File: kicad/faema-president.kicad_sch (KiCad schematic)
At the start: 18 parts, among them J1 AC_INPUT, J2 CALDEIRA_2400W, J3 PT100_CALDEIRA, J6 PT100_GRUPO, J7 SONDA_NIVEL, U1 ESP32-S3 Mini, U2 HLK-PM05, U3 AMS1117-3.3, U4 MAX31865_CALDEIRA, U5 DS3231, U6 MAX31865_GRUPO

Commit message: Rev.5: SPEC revisada + esquemático KiCad gerado
- SPEC.md Rev.5: source of truth migrado para KiCad, display ILI9341 2.4"
  em caixinha externa, SSR drive com 2N7002 (Q1+R_gate), scheduler só
  aquecimento, seção de segurança, J2/J9 adicionados, snubber removido
- kicad_sch Rev.5: 10244 linhas, 95 componentes — novos símbolos (NMOS,
  Fuse, MOV, Conn 5/6/8pin), Q1/R_gate/F1/RV1/passivos/conectores gerados,
  R7 atualizado 100R→220R, global labels para todos os sinais
- gen_sch.py: script Python reproduzível para regenerar o esquemático

Co-Authored-By: Claude Sonnet 4.6 <noreply@anthropic.com>
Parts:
- added C1, C2: 10u/16V, symbol faema:C
- added C10, C11, C12, C3, C4, C7, C8, C9: 100n, symbol faema:C
- added F1: T16A, symbol faema:Fuse
- added J5: ILI9341_DISP, symbol faema:Conn_8pin
- added J8: PRESET_BTNS, symbol faema:Conn_6pin
- added J9: ENCODER, symbol faema:Conn_5pin
- added Q1: 2N7002, symbol faema:NMOS_GSD
- added R12, R13, R14: 10k, symbol faema:R
- added R2, R3: 4k7, symbol faema:R
- added RV1: S14K275, symbol faema:MOV
- added R_gate: 100R, symbol faema:R
- added Rref, Rref2: 430R 0.1%, symbol faema:R
- R7: value 100R -> 220R
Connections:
- net I2C_SCL: now also R3.2
- net I2C_SDA: now also R2.2
- net SPI_MOSI: now also J5.3 (Pin_3)
- net SPI_SCK: now also J5.2 (Pin_2)
- net +5V: now reaches R7.1
- net +5V: now also C1.1, C3.1
- net GND: now reaches R9.2
- net GND: now also C1.2, C10.2, C12.2, C2.2, C3.2, C4.2, C8.2, C9.2, J5.7 (Pin_7), J8.1 (Pin_1), J8.2 (Pin_2), J9.1 (Pin_1), Q1.2 (D)
- new net +3V3: C10.1, C12.1, C2.1, C4.1, C8.1, C9.1, J5.1 (Pin_1), J5.8 (Pin_8), J8.3 (Pin_3), J9.2 (Pin_2), R12.1, R13.1, R14.1, R2.1, R3.1
- new net BTN1: J8.6 (Pin_6), R12.2
- new net BTN2: J8.5 (Pin_5), R13.2
- new net BTN3: J8.4 (Pin_4), R14.2
- new net CS_DISP: J5.6 (Pin_6)
- new net DC_DISP: J5.4 (Pin_4)
- new net ENC_CLK: J9.5 (Pin_5)
- new net ENC_DT: J9.4 (Pin_4)
- new net ENC_SW: J9.3 (Pin_3)
- new net FORCE_PLUS_U4: Rref.2
- new net FORCE_PLUS_U6: Rref2.2
- new net Q1_GATE: Q1.1 (G), R_gate.2
- new net REFIN_PLUS_U4: Rref.1
- new net REFIN_PLUS_U6: Rref2.1
- new net RST_DISP: J5.5 (Pin_5)
- new net RTDIN_MINUS_U4: C7.2
- new net RTDIN_MINUS_U6: C11.2
- new net RTDIN_PLUS_U4: C7.1
- new net RTDIN_PLUS_U6: C11.1
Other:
- note added: "FAEMA PRESIDENT - Rev.5 Conectar nets com mesmo nome global label. Ver CLAUDE.md para especificação completa."
- note removed: "FAEMA PRESIDENT - Rev.4 Conectar nets com mesmo nome global label. TODO: adicionar passivos (Rref, bypass caps, pull-ups) Ver CONTEXT.md para especificação completa."

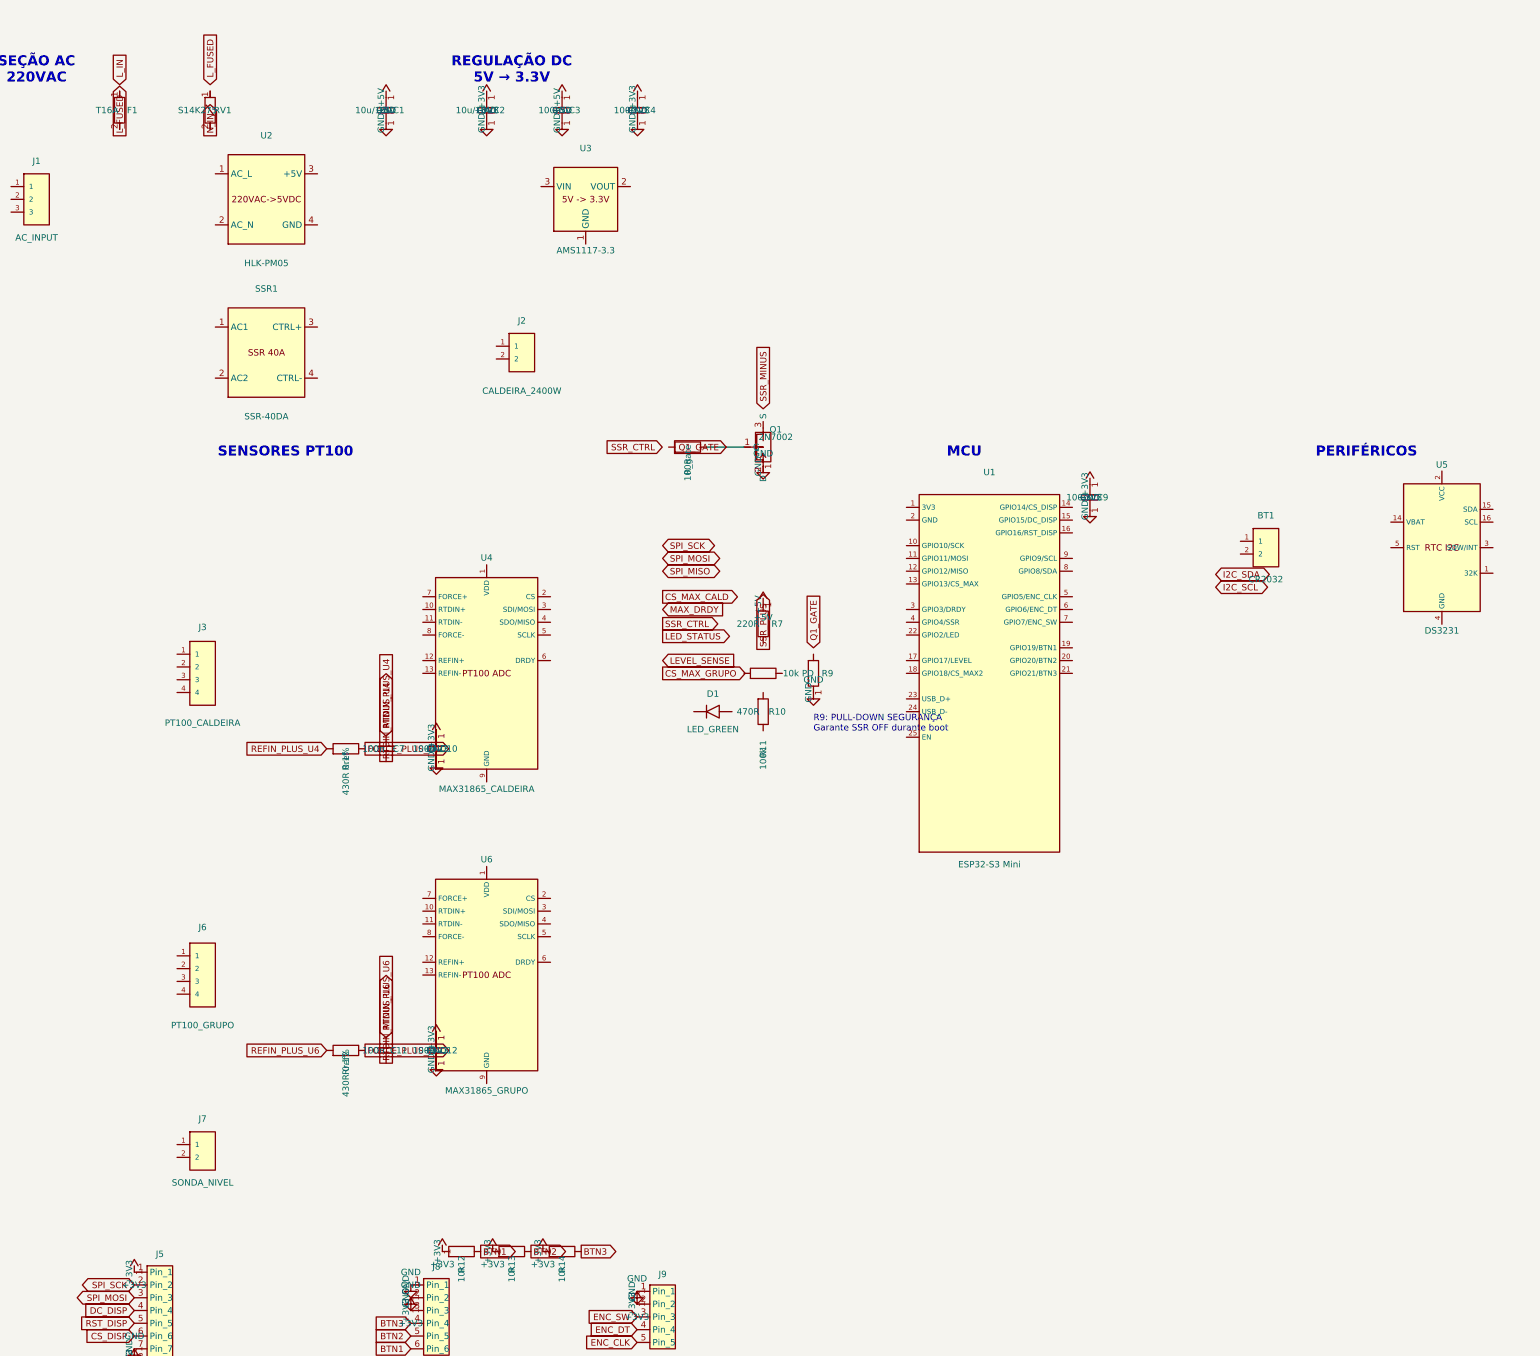
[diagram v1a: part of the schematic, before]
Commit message: Rev.5: corrigir sobreposições no esquemático — layout melhorado
- R9 movido de (185,140) para (192,112): saiu da zona dos ICs principais
- R11 movido de (175,140) para (48,248): agora perto de J7 (sonda nível)
- R7 movido de (175,130) para (188,70): no bloco de drive do SSR
- R10/D1 movidos para (256,232)/(240,232): abaixo do ESP32
- C1-C4 movidos para x=175–220: espaçamento adequado no topo
- U1 ESP32 movido de (220,140) para (295,160): área própria à direita
- C9 bypass movido para perto do ESP32 (295,110)
- Adicionadas conexões para R11 (LEVEL_SENSE + 3.3V)
- Adicionadas conexões para D1+R10 (LED_STATUS + GND)

Co-Authored-By: Claude Sonnet 4.6 <noreply@anthropic.com>
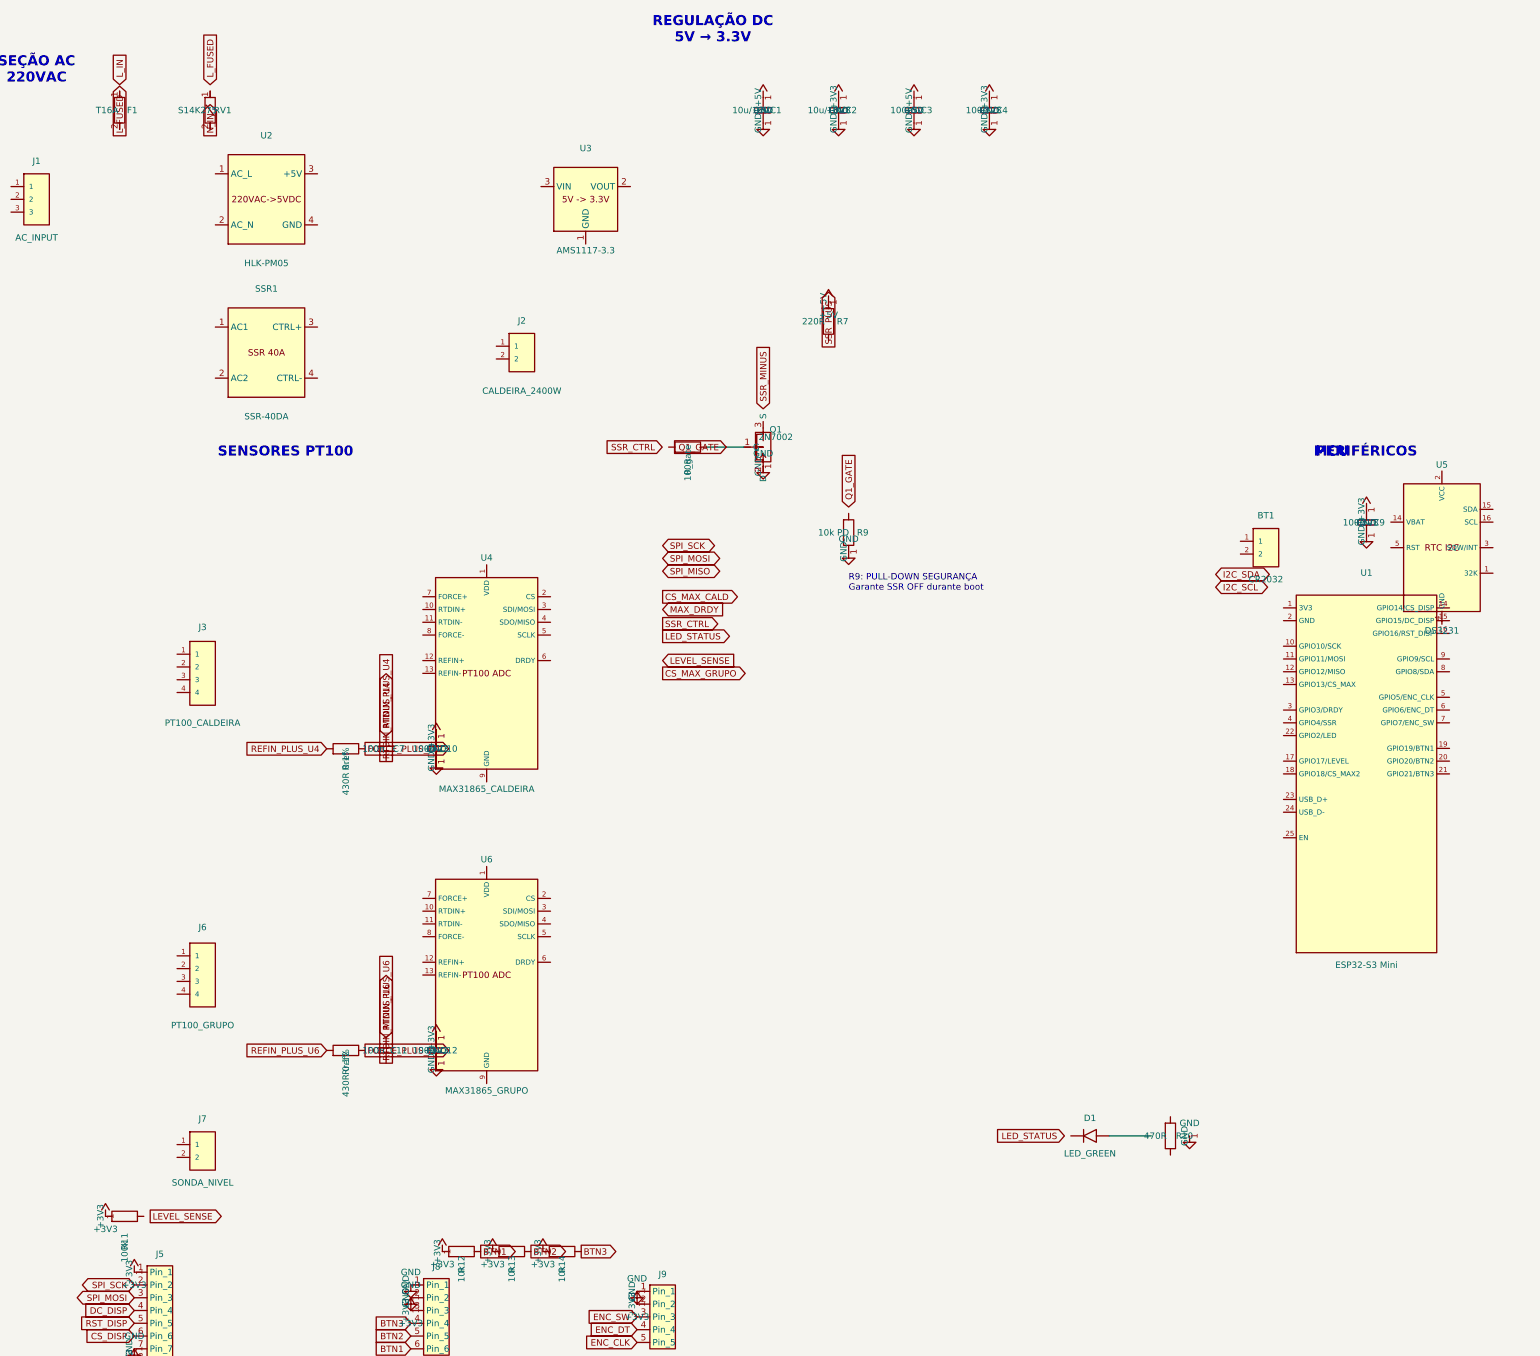
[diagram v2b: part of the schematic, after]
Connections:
- net +3V3: now also R11.1
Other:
- moved on the sheet: C1, C2, C3, C4, C9, D1, R10, R11, R7, R9, U1
